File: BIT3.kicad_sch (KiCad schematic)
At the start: 48 parts, among them J1 Conn_02x04_Odd_Even, J2 Conn_01x02_Pin, J3 Conn_01x04_Socket, J4 Conn_02x02_Odd_Even, Q1 2SC1815, SW1 SW_SPDT, SW2 SW_Push, SW3 SW_Push, U2 FODM217A, U3 FODM217A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

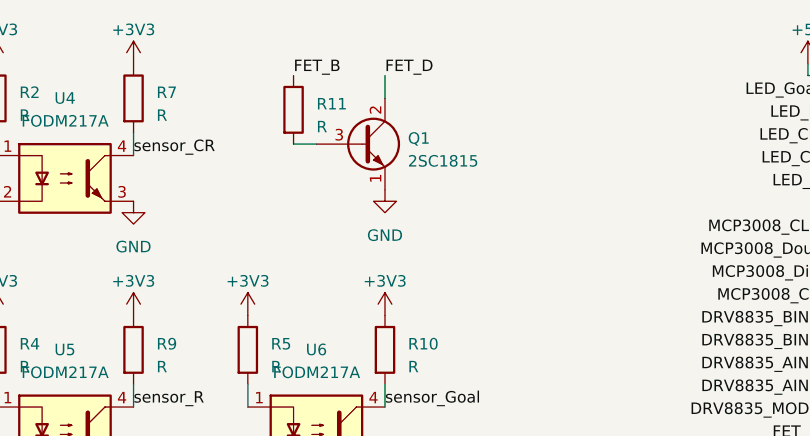
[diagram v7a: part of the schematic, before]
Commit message: 赤外線 LED 用トランジスタを変更
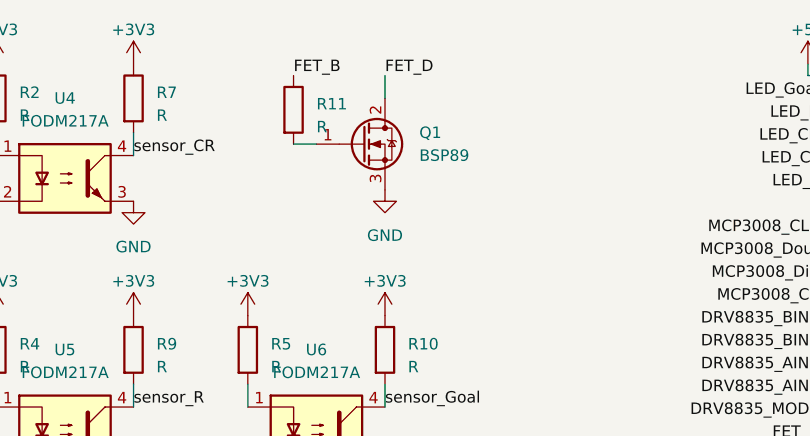
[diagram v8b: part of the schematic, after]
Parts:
- removed Q1: 2SC1815, Package_TO_SOT_THT:TO-92_Inline, symbol Transistor_BJT:2SC1815
- added Q1: BSP89, Package_TO_SOT_THT:TO-220-3_Vertical, symbol Transistor_FET:BSP89
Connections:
- net FET_D: now also Q1.2 (D)
- net GND: now also Q1.3 (S)
- net at R11.2: now also Q1.1 (G)
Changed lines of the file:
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@@
+    )
+  )
+  (symbol (lib_id "Transistor_FET:BSP89") (at 96.52 76.2 0) (unit 1)
+    (in_bom yes) (on_board yes) (dnp no) (fields_autoplaced)
+    (property "Reference" "Q1" (at 102.87 74.93 0)
+      (effects (font (size 1.27 1.27)) (justify left))
+    )
+    (property "Value" "BSP89" (at 102.87 77.47 0)
+      (effects (font (size 1.27 1.27)) (justify left))
+    )
+    (property "Footprint" "Package_TO_SOT_THT:TO-220-3_Vertical" (at 101.6 78.105 0)
+      (effects (font (size 1.27 1.27) italic) (justify left) hide)
+    )
+    (property "Datasheet" "https://www.infineon.com/dgdl/Infineon-BSP89-DS-v02_02-en.pdf?fileId=db3a30433b47825b013b4b8a07f90d55" (at 96.52 76.2 0)
+      (effects (font (size 1.27 1.27)) (justify left) hide)
+    )
+    (pin "1")
+    (pin "2")
+    (pin "3")
+    (instances
+      (project "BIT3"
+        (path "/e911d5a5-765c-4e39-aa6a-9a13739432fd"
+          (reference "Q1") (unit 1)
+        )
+      )
     )
   )
@@
         )
       )
-    )
-  )
-  (symbol (lib_id "Transistor_BJT:2SC1815") (at 96.52 76.2 0) (unit 1)
-    (in_bom yes) (on_board yes) (dnp no) (fields_autoplaced)
-    (property "Reference" "Q1" (at 101.6 75.565 0)
-      (effects (font (size 1.27 1.27)) (justify left))
-    )
-    (property "Value" "2SC1815" (at 101.6 78.105 0)
-      (effects (font (size 1.27 1.27)) (justify left))
-    )
-    (property "Footprint" "Package_TO_SOT_THT:TO-92_Inline" (at 101.6 78.105 0)
-      (effects (font (size 1.27 1.27) italic) (justify left) hide)
-    )
-    (property "Datasheet" "https://media.digikey.com/pdf/Data%20Sheets/Toshiba%20PDFs/2SC1815.pdf" (at 96.52 76.2 0)
-      (effects (font (size 1.27 1.27)) (justify left) hide)
-    )
-    (pin "1")
-    (pin "2")
-    (pin "3")
-    (instances
-      (project "BIT3"
-        (path "/e911d5a5-765c-4e39-aa6a-9a13739432fd"
-          (reference "Q1") (unit 1)
-        )
-      )
